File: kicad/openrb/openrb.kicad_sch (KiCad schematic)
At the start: 56 parts, among them U1 RP2040, U2 CH334R, U4 RT9080-33, U5 W25Q16JV, U6 H11L1, X1 12MHz, X2 12MHz

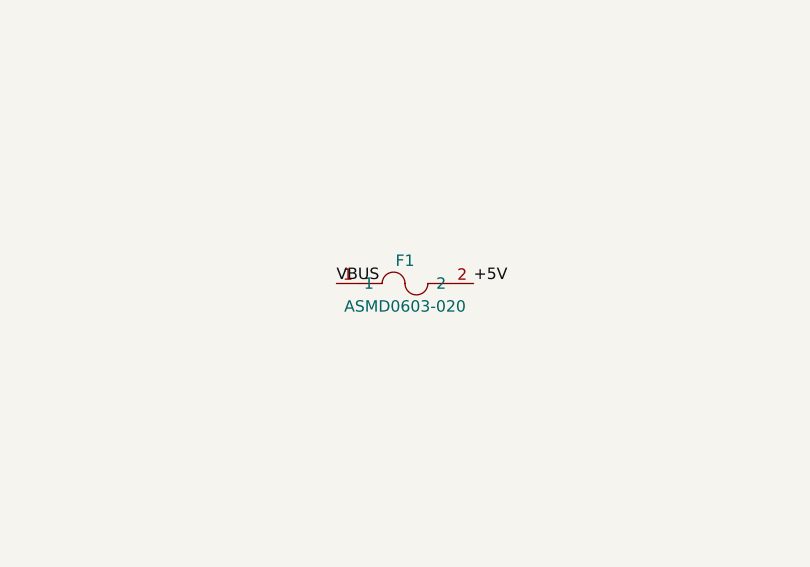
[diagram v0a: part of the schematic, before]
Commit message: Generate editable KiCad schematic from verified netlist + LCSC symbols
Schematic now loads in KiCad 10, exports a netlist, and renders. All 56
components placed with their exact LCSC/EasyEDA symbols (pulled by part
number) and matching footprints; connectivity via net labels at true pin
endpoints. Spot-checked critical nets against RECONSTRUCTION.md (USB device/
host, hub->ports, MIDI, reset/boot, power rails) — all match. Added project
sym/fp-lib-tables. Remaining ERC items are pin-type-strictness warnings
(PWR_FLAG vs bidirectional), not wiring errors.
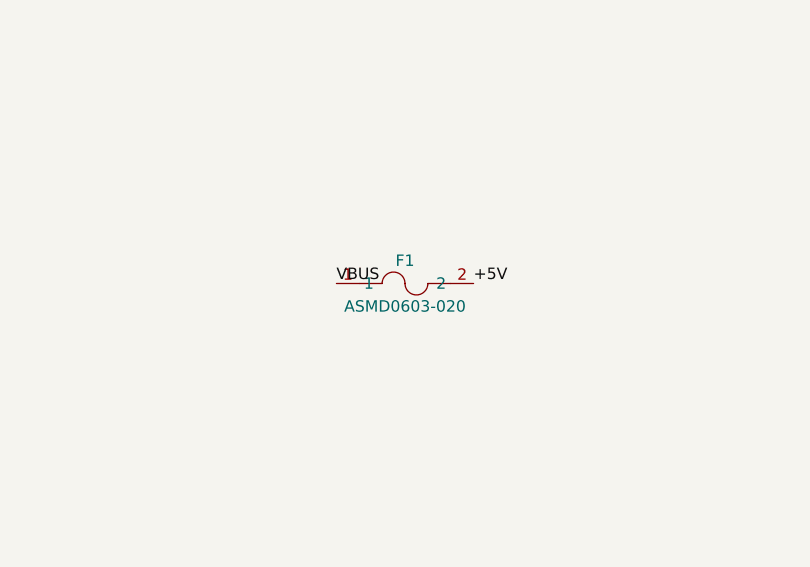
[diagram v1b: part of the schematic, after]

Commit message: Split schematic into 3 pages grouped by subsection
Hierarchical project: root sheet + USB / MCU / MIDI child pages, mirroring
the original schematic's organization. Components grouped under titled
subsections (USB-C/ESD, hub, host ports, RP2040, decoupling, flash, osc,
regulator, reset, prog, status LEDs, MIDI). Cross-sheet connectivity via
global labels; netlist verified identical to the single-sheet version
(56 components, 78 nets, same node membership). gen_multi.py regenerates it.
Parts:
- removed BOOT: BOOT, openrb:KEY-SMD_4P-L4.5-W4.5-P3.00-LS6.5-TL, symbol openrb:PTS647SM38SMTR2LFS
- removed C1, C2: 10uF, openrb:C0402, symbol openrb:GRM155R61A106ME44D
- removed C10, C11, C3, C4, C5, C6, C8, C9: 100nF, openrb:C0402, symbol openrb:CL05B104KB54PNC
- removed C12, C13, C14, C17: 100uF, openrb:CASE-B_3528, symbol openrb:TAJB107K006RNJ
- removed C15, C16: 15pF, openrb:C0603, symbol openrb:CL10C150JB8NNNC
- removed C18, C19, C20, C7: 1uF, openrb:C0402, symbol openrb:CL05A105KQ5NNNC
- removed D1: 1N4148WS, openrb:SOD-323_L1.8-W1.3-LS2.5-RD, symbol openrb:1N4148WS_C402214
- removed D2: USBLC6-2SC6, openrb:SOT-23-6_L2.9-W1.6-P0.95-LS2.8-BL, symbol openrb:USBLC6-2SC6_C2827654
- removed F1: ASMD0603-020, openrb:F0603, symbol openrb:ASMD0603-020
- removed H2: PWR_IN, openrb:HDR-TH_2P-P2.54-V-F, symbol openrb:Header-Female-2.54_1x2
- removed LED_3V3: 3V3, openrb:LED0603-RD, symbol openrb:19-217_R6C-AL1M2VY_3T
- removed LED_5V: 5V, openrb:LED0603-RD, symbol openrb:19-217_R6C-AL1M2VY_3T
- removed LED_AUTH: AUTH, openrb:LED0603-RD, symbol openrb:19-217_R6C-AL1M2VY_3T
- removed MIDI: CP-2350, symbol openrb:MIDI_TRS
- removed R1, R3: 5.1k, openrb:R0402, symbol openrb:0402WGF2200TCE
- removed R10, R11, R12, R7: 1k, openrb:R0402, symbol openrb:0402WGF2200TCE
- removed R13, R9: 10k, openrb:R0402, symbol openrb:0402WGF2200TCE
- removed R14, R15: 22, openrb:R0402, symbol openrb:0402WGF2200TCE
- removed R2: 220, openrb:R0402, symbol openrb:0402WGF2200TCE
- removed R4, R6, R8: 470, openrb:R0402, symbol openrb:0402WGF2200TCE
- removed RESET: RESET, openrb:KEY-SMD_4P-L4.5-W4.5-P3.00-LS6.5-TL, symbol openrb:PTS647SM38SMTR2LFS
- removed SWD1: SWD, openrb:HDR-TH_3P-P2.54-V-F, symbol openrb:22025403P00CKMT
- removed U1: RP2040, openrb:LQFN-56_L7.0-W7.0-P0.4-EP, symbol openrb:RP2040
- removed U2: CH334R, openrb:QSOP-16_L4.9-W3.9-P0.64-LS6.0-BL, symbol openrb:CH334R
- removed U4: RT9080-33, openrb:TSOT-23-5_L2.9-W1.6-P0.95-LS2.8-BL, symbol openrb:RT9080-33GJ5
- removed U5: W25Q16JV, openrb:USON-8_L3.0-W2.0-P0.50-BL-EP, symbol openrb:W25Q16JVUXIQ
- removed U6: H11L1, openrb:DIP-6_L8.5-W6.4-P2.54-LS7.6-BL, symbol openrb:H11L1
- removed UART: UART, openrb:HDR-TH_3P-P2.54-V-F, symbol openrb:22025403P00CKMT
- removed USB0, USB1: UB1112C, openrb:USB-A-TH_UB1112C-8FDE-4F, symbol openrb:UB1112C-8FDE-4F
- removed USBC1: USB-C, openrb:USB-C_SMD-TYPE-C-31-M-12_1, symbol openrb:TYPE-C-31-M-12
- removed X1, X2: 12MHz, openrb:CRYSTAL-SMD_4P-L3.2-W2.5-BL, symbol openrb:X322512MSB4SI
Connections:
- no-connect marks 27 -> 0
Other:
- added sheet MCU (mcu.kicad_sch)
- added sheet MIDI (midi.kicad_sch)
- added sheet USB (usb.kicad_sch)
